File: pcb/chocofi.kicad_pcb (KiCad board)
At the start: 2 copper layers, 111.3 x 90 mm, 60 parts, among them J1 MJ-4PP-9, J2 OLED, J3 Conn_01x02_Female, SW1 SW_SPDT, SW10 SW_PUSH, SW11 SW_PUSH, SW12 SW_PUSH, SW14 SW_PUSH, SW15 SW_PUSH, SW16 SW_PUSH, SW17 SW_PUSH, SW18 SW_PUSH, SW19 SW_PUSH, SW2 SW_PUSH, SW2 SW_SPDT, SW20 SW_PUSH, SW21 SW_PUSH, SW3 SW_PUSH, SW4 SW_PUSH, SW5 SW_PUSH, SW6 SW_PUSH, SW8 SW_PUSH, SW9 SW_PUSH, U1 ProMicro

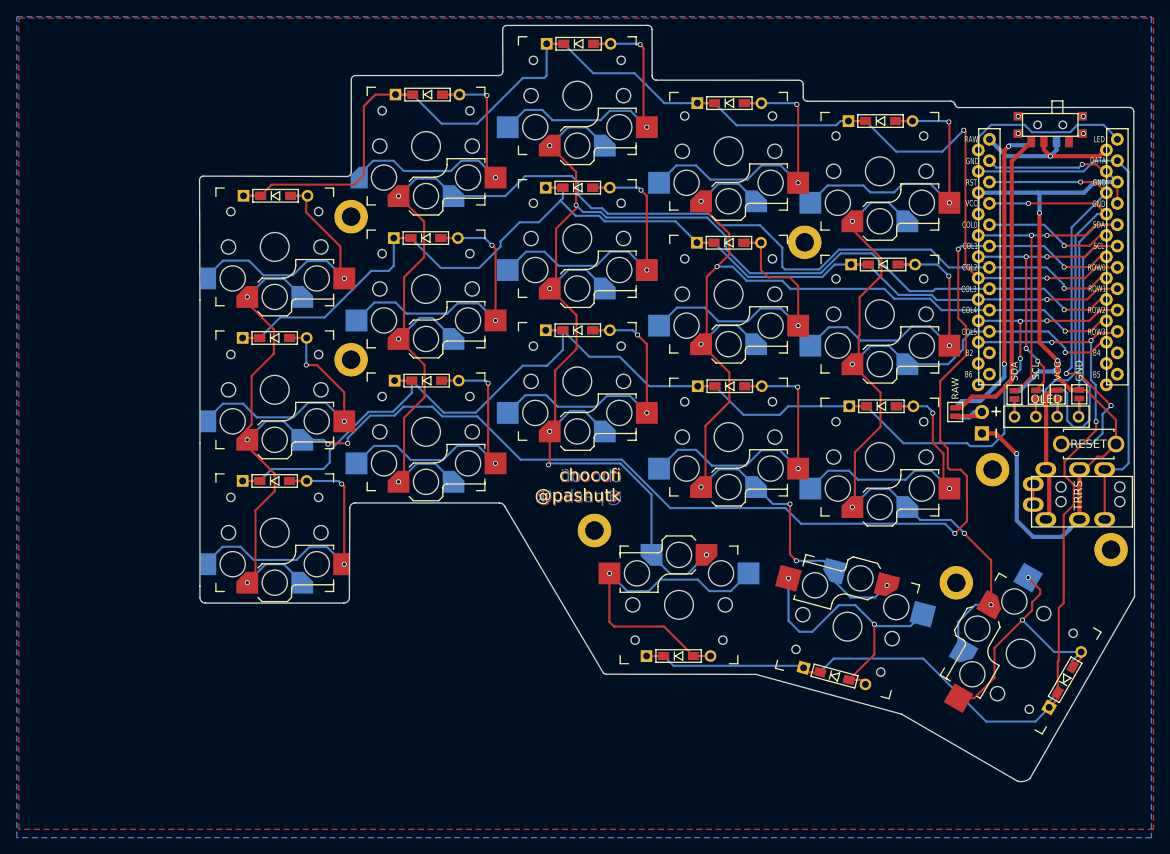
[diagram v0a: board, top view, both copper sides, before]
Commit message: swap switch footprints for choc mini ones + reroute
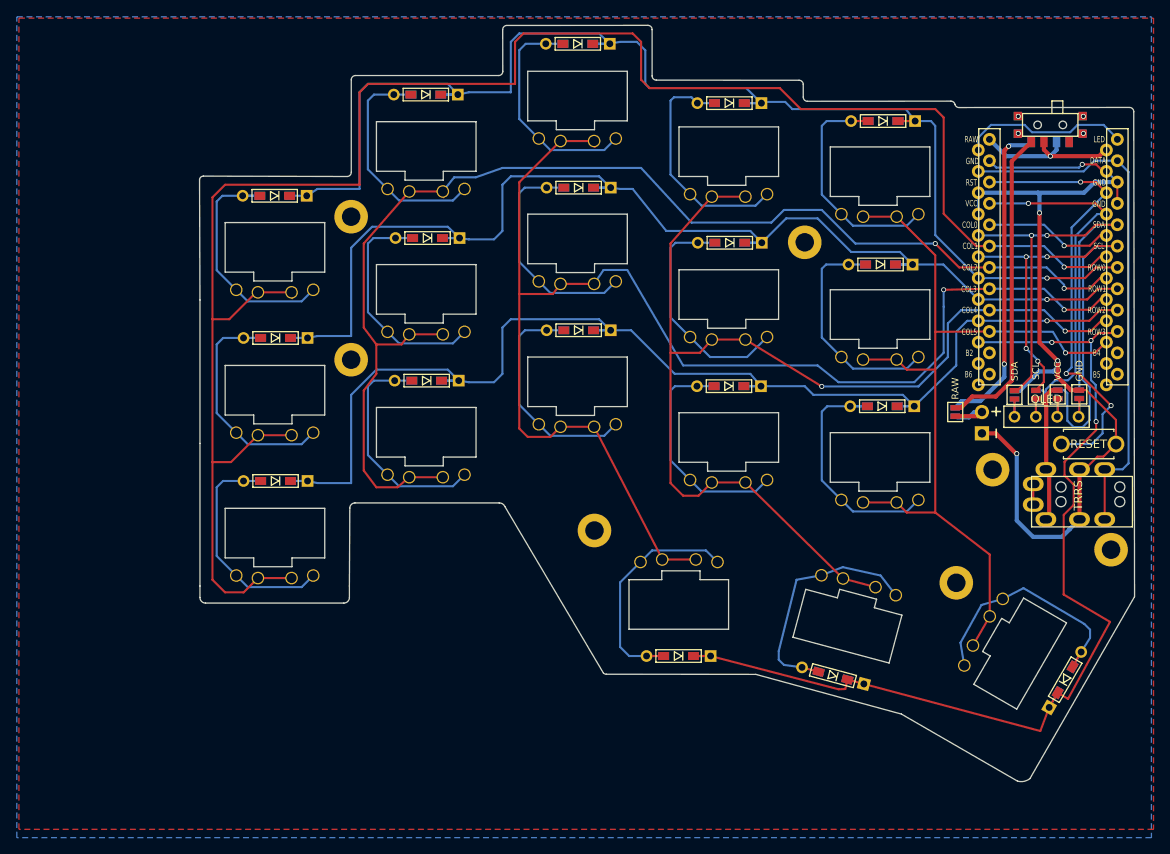
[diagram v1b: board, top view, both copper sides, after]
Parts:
- D10, D11, D12, D14, D15, D16, D17, D18, D19, D2, D20, D3, D4, D5, D6, D8, D9: moved to B.Cu
- SW10, SW11, SW12, SW14, SW15, SW16, SW17, SW18, SW19, SW2, SW20, SW21, SW3, SW4, SW5, SW6, SW8, SW9: footprint keyswitches:Kailh_socket_PG1350_reversible -> wonkyshit:SW_Kailh_Choc_Mini_1.00u_reversible
- moved D12 0.30 mm to (158.0, 72.5), turned to 180 degrees
- moved D6 0.30 mm to (158.3, 55.4), turned to 180 degrees
- moved D3 0.20 mm to (103.9, 52.3), turned to 180 degrees
- moved D9 0.20 mm to (104.1, 69.3), turned to 180 degrees
- moved D20 0.19 mm to (152.3, 121.4), turned to 165 degrees
- moved D18 0.10 mm to (158.2, 89.4), turned to 180 degrees
- moved D10 0.10 mm to (122.1, 63.3), turned to 180 degrees
- moved D14 0.10 mm to (86.0, 98.2), turned to 180 degrees
- moved D16 0.10 mm to (122.1, 80.3), turned to 180 degrees
- moved D2 0.10 mm to (85.9, 64.3), turned to 180 degrees
- moved D4 0.10 mm to (122.0, 46.2), turned to 180 degrees
- moved D8 0.10 mm to (86.0, 81.2), turned to 180 degrees
- moved D11 0.10 mm to (140.1, 69.9), turned to 180 degrees
- moved D17 0.10 mm to (140.0, 87.0), turned to 180 degrees
- turned D15 to 180 degrees
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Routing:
- net col1: track 205.3 -> 223.5 mm, vias 8 -> 1
- net Net-(D19-Pad2): track 41.0 -> 27.0 mm, vias 1 -> 0
- net col5: track 114.9 -> 101.1 mm, vias 6 -> 1
- net Net-(D17-Pad2): track 38.0 -> 27.3 mm, vias 2 -> 0
- net Net-(D14-Pad2): track 37.6 -> 27.3 mm, vias 2 -> 0
- net row2: track 156.9 -> 146.7 mm, vias 3 -> 1
- net Net-(D10-Pad2): track 37.4 -> 27.3 mm, vias 2 -> 0
- net Net-(D6-Pad2): track 37.2 -> 27.5 mm, vias 2 -> 0
- net Net-(D9-Pad2): track 36.9 -> 27.4 mm, vias 2 -> 0
- net Net-(D12-Pad2): track 36.7 -> 27.2 mm, vias 2 -> 0
- net Net-(D16-Pad2): track 36.7 -> 27.3 mm, vias 2 -> 0
- net Net-(D5-Pad2): track 37.4 -> 28.1 mm, vias 2 -> 0
- net Net-(D4-Pad2): track 36.4 -> 27.3 mm, vias 2 -> 0
- net Net-(D15-Pad2): track 36.0 -> 27.3 mm, vias 2 -> 0
- net Net-(D20-Pad2): track 36.8 -> 28.1 mm, vias 2 -> 0
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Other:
- board text removed: "chocofi @pashutk"

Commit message: remove diode through-holes, move diode pads to led-hole
through hole diodes obv. don't fit on the side the switches are on,
and are taller than the feet on the other side.
we're looking for thinness here, so through-hole diodes are out

moved the diode pads so the (smd) diodes sit in the void choc minis have
for LEDs

also using the adjacent foot through-holes of the switch as a via for
the diode pads
those feet aren't electrically connected to anything so that should be
fine
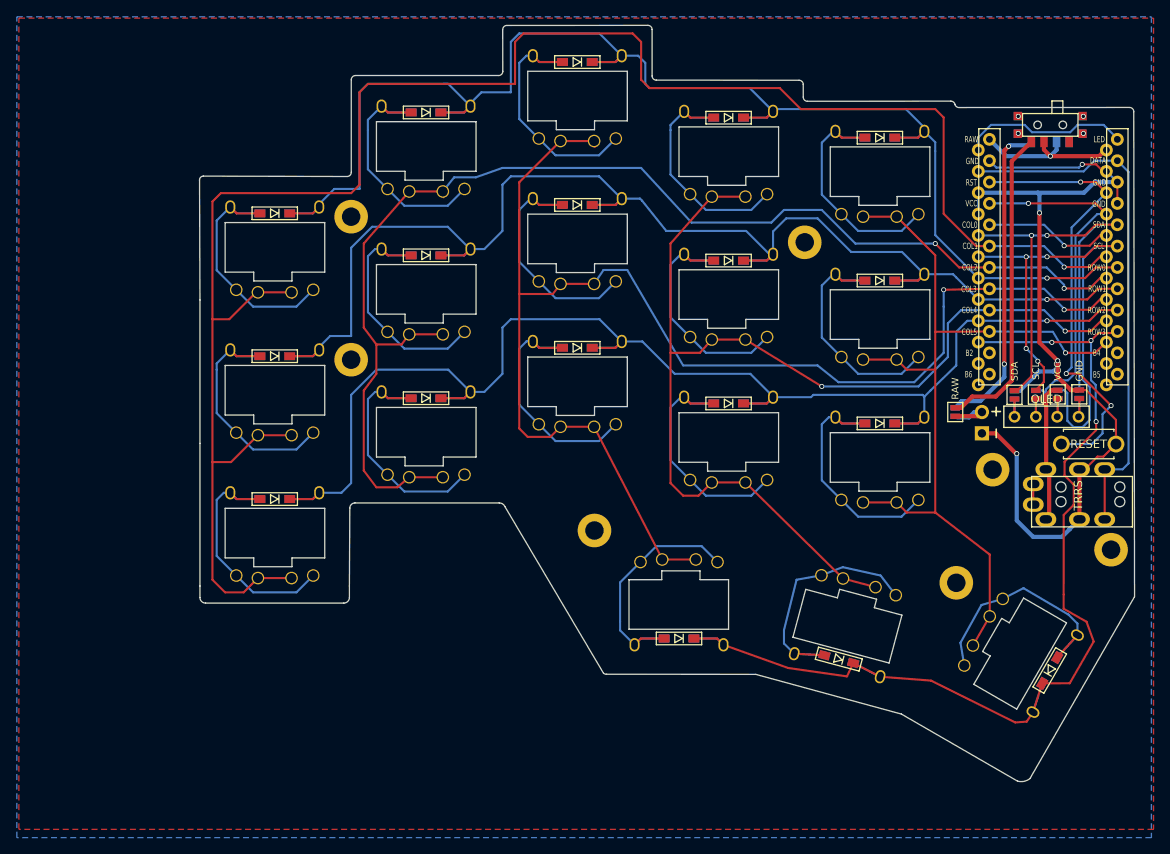
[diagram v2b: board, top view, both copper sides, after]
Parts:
- moved D8 2.17 mm to (85.9, 83.4)
- moved D4 2.17 mm to (121.9, 48.4)
- moved D14 2.15 mm to (85.9, 100.4)
- moved D21 2.14 mm to (178.1, 120.8)
- moved D3 2.13 mm to (103.9, 54.4)
- moved D11 2.12 mm to (139.9, 72.0)
- moved D15 2.09 mm to (103.9, 88.4)
- moved D16 2.09 mm to (121.9, 82.4)
- moved D2 2.09 mm to (85.9, 66.4)
- moved D20 2.09 mm to (153.0, 119.4)
- moved D19 2.09 mm to (134.0, 117.0)
- moved D9 2.07 mm to (103.9, 71.4)
- moved D18 2.06 mm to (157.9, 91.4)
- moved D10 2.06 mm to (121.9, 65.4)
- moved D17 2.06 mm to (139.9, 89.0)
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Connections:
- SW10 pad : (no net) -> row1
- SW11 pad : (no net) -> row1
- SW12 pad : (no net) -> row1
- SW14 pad : (no net) -> row2
- SW15 pad : (no net) -> row2
- SW16 pad : (no net) -> row2
- SW17 pad : (no net) -> row2
- SW18 pad : (no net) -> row2
- SW19 pad : (no net) -> Net-(D19-Pad2)
- SW2 pad : (no net) -> row0
- SW20 pad : (no net) -> Net-(D20-Pad2)
- SW21 pad : (no net) -> row3
- SW3 pad : (no net) -> row0
- SW4 pad : (no net) -> row0
- SW5 pad : (no net) -> row0
- SW6 pad : (no net) -> row0
- SW8 pad : (no net) -> row1
- SW9 pad : (no net) -> row1
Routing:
- net row1: track 144.1 -> 165.5 mm
- net row2: track 146.7 -> 166.5 mm
- net row0: track 156.8 -> 175.7 mm
- net Net-(D15-Pad2): track 27.3 -> 30.4 mm
- net Net-(D4-Pad2): track 27.3 -> 30.4 mm
- net Net-(D14-Pad2): track 27.3 -> 30.4 mm
- net Net-(D16-Pad2): track 27.3 -> 30.4 mm
- net Net-(D9-Pad2): track 27.4 -> 30.4 mm
- net Net-(D12-Pad2): track 27.2 -> 30.1 mm
- net Net-(D19-Pad2): track 27.0 -> 29.9 mm
- net Net-(D17-Pad2): track 27.3 -> 30.1 mm
- net Net-(D10-Pad2): track 27.3 -> 30.1 mm
- net Net-(D3-Pad2): track 27.2 -> 30.0 mm
- net Net-(D6-Pad2): track 27.5 -> 30.1 mm
- net row3: track 123.5 -> 125.6 mm
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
